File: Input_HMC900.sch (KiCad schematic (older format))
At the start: 7 parts

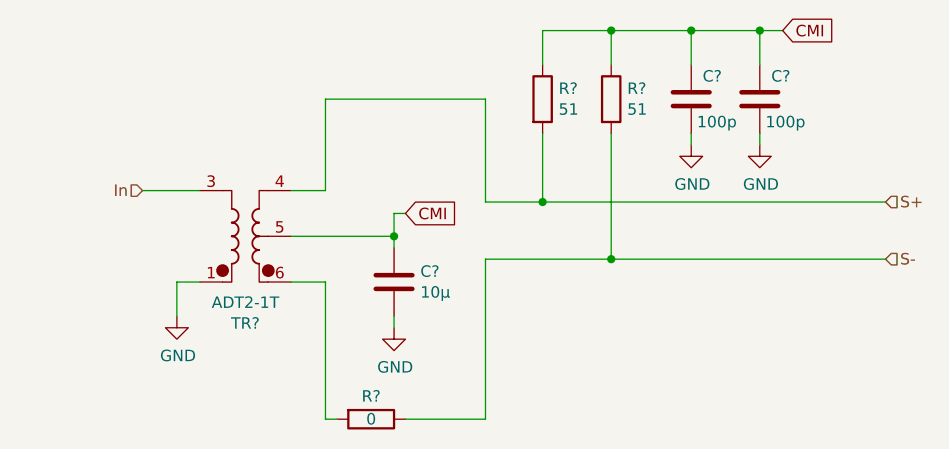
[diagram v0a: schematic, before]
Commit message: Corrected errors from single ended transition
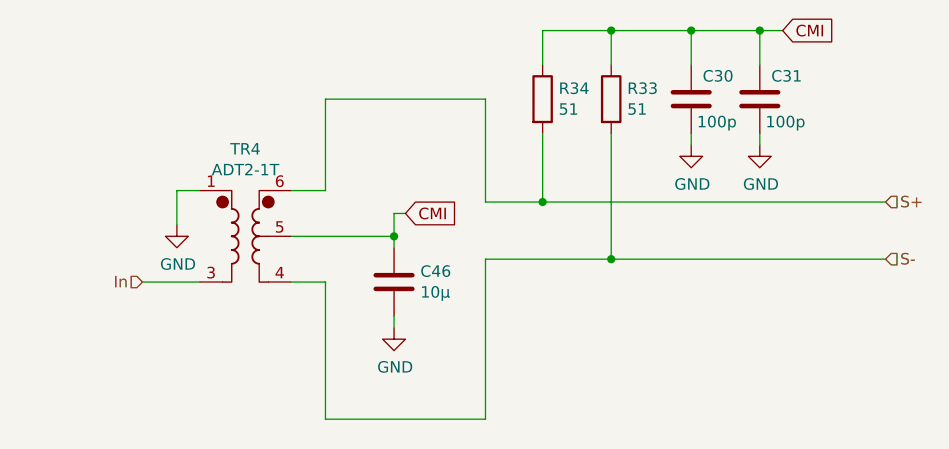
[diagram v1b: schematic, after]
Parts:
- removed R44: 0, Resistor_SMD:R_0402_1005Metric, symbol Device:R
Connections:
- net S+: now also TR4.6; no longer TR4.4
- net S-: now also TR4.4
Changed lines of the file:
@@
 $Descr A4 11693 8268
 encoding utf-8
-Sheet 4 7
+Sheet 5 7
 Title ""
 Date ""
@@
 AR Path="/60D21B6E/6110419F/60F9EBFF" Ref="C30"  Part="1"
 AR Path="/60D21B6E/61121120/60F9EBFF" Ref="C28"  Part="1"
-AR Path="/60D21B6E/60F52DEE/60F9EBFF" Ref="C?"  Part="1"
-F 0 "C?" H 6150 2800 50  0000 R CNN
+AR Path="/60D21B6E/60F52DEE/60F9EBFF" Ref="C30"  Part="1"
+F 0 "C30" H 6150 2800 50  0000 R CNN
 F 1 "100p" H 6175 3000 50  0000 R CNN
 F 2 "Capacitor_SMD:C_0402_1005Metric" H 6238 2750 50  0001 C CNN
@@
 AR Path="/60D21B6E/6110419F/60F9EC14" Ref="#PWR0135"  Part="1"
 AR Path="/60D21B6E/61121120/60F9EC14" Ref="#PWR0131"  Part="1"
-AR Path="/60D21B6E/60F52DEE/60F9EC14" Ref="#PWR?"  Part="1"
-F 0 "#PWR?" H 6200 2850 50  0001 C CNN
+AR Path="/60D21B6E/60F52DEE/60F9EC14" Ref="#PWR0135"  Part="1"
+F 0 "#PWR0135" H 6200 2850 50  0001 C CNN
 F 1 "GND" H 6205 2927 50  0000 C CNN
 F 2 "" H 6200 3100 50  0001 C CNN
@@
 	1    0    0    -1
 $EndComp
-$Comp
-L Device:R R?
-U 1 1 60F9EC7E
-P 4800 4300
-AR Path="/60D21B6E/60F9EC7E" Ref="R?"  Part="1"
-AR Path="/60D21B6E/60D894BC/60F9EC7E" Ref="R?"  Part="1"
-AR Path="/60D21B6E/6110419F/60F9EC7E" Ref="R44"  Part="1"
-AR Path="/60D21B6E/61121120/60F9EC7E" Ref="R43"  Part="1"
-AR Path="/60D21B6E/60F52DEE/60F9EC7E" Ref="R?"  Part="1"
-F 0 "R?" V 4700 4300 50  0000 C CNN
-F 1 "0" V 4800 4300 50  0000 C CNN
-F 2 "Resistor_SMD:R_0402_1005Metric" V 4730 4300 50  0001 C CNN
-F 3 "~" H 4800 4300 50  0001 C CNN
-	1    4800 4300
-	0    1    1    0
-$EndComp
 Wire Wire Line
 	5300 3600 5300 4300
-Wire Wire Line
-	4600 4300 4650 4300
-Wire Wire Line
-	4950 4300 5300 4300
 Wire Wire Line
 	5300 3600 5850 3600
@@
 AR Path="/60D21B6E/6110419F/60F9EC05" Ref="C31"  Part="1"
 AR Path="/60D21B6E/61121120/60F9EC05" Ref="C29"  Part="1"
-AR Path="/60D21B6E/60F52DEE/60F9EC05" Ref="C?"  Part="1"
-F 0 "C?" H 6450 2800 50  0000 R CNN
+AR Path="/60D21B6E/60F52DEE/60F9EC05" Ref="C31"  Part="1"
+F 0 "C31" H 6450 2800 50  0000 R CNN
 F 1 "100p" H 6475 3000 50  0000 R CNN
 F 2 "Capacitor_SMD:C_0402_1005Metric" H 6538 2750 50  0001 C CNN
@@
 AR Path="/60D21B6E/6110419F/6100BC4B" Ref="#PWR0138"  Part="1"
 AR Path="/60D21B6E/61121120/6100BC4B" Ref="#PWR0134"  Part="1"
-AR Path="/60D21B6E/60F52DEE/6100BC4B" Ref="#PWR?"  Part="1"
-F 0 "#PWR?" H 6500 2850 50  0001 C CNN
+AR Path="/60D21B6E/60F52DEE/6100BC4B" Ref="#PWR0136"  Part="1"
+F 0 "#PWR0136" H 6500 2850 50  0001 C CNN
 F 1 "GND" H 6505 2927 50  0000 C CNN
 F 2 "" H 6500 3100 50  0001 C CNN
@@
 Wire Wire Line
 	5850 3600 7050 3600
-Text HLabel 3800 3300 0    50   Input ~ 0
+Text HLabel 3800 3700 0    50   Input ~ 0
 In
 Text HLabel 7050 3350 2    50   Input ~ 0
@@
 AR Path="/60D21B6E/6110419F/60F9EBF5" Ref="R33"  Part="1"
 AR Path="/60D21B6E/61121120/60F9EBF5" Ref="R32"  Part="1"
-AR Path="/60D21B6E/60F52DEE/60F9EBF5" Ref="R?"  Part="1"
-F 0 "R?" H 5920 2946 50  0000 L CNN
+AR Path="/60D21B6E/60F52DEE/60F9EBF5" Ref="R33"  Part="1"
+F 0 "R33" H 5920 2946 50  0000 L CNN
 F 1 "51" H 5920 2855 50  0000 L CNN
 F 2 "Resistor_SMD:R_0402_1005Metric" V 5780 2900 50  0001 C CNN
@@
 AR Path="/60D21B6E/6110419F/60F9EC23" Ref="R34"  Part="1"
 AR Path="/60D21B6E/61121120/60F9EC23" Ref="R31"  Part="1"
-AR Path="/60D21B6E/60F52DEE/60F9EC23" Ref="R?"  Part="1"
-F 0 "R?" H 5620 2946 50  0000 L CNN
+AR Path="/60D21B6E/60F52DEE/60F9EC23" Ref="R34"  Part="1"
+F 0 "R34" H 5620 2946 50  0000 L CNN
 F 1 "51" H 5620 2855 50  0000 L CNN
 F 2 "Resistor_SMD:R_0402_1005Metric" V 5480 2900 50  0001 C CNN
@@
 AR Path="/60D21B6E/6110419F/60F9EC42" Ref="#PWR0137"  Part="1"
 AR Path="/60D21B6E/61121120/60F9EC42" Ref="#PWR0133"  Part="1"
-AR Path="/60D21B6E/60F52DEE/60F9EC42" Ref="#PWR?"  Part="1"
-F 0 "#PWR?" H 4900 3650 50  0001 C CNN
+AR Path="/60D21B6E/60F52DEE/60F9EC42" Ref="#PWR0137"  Part="1"
+F 0 "#PWR0137" H 4900 3650 50  0001 C CNN
 F 1 "GND" H 4905 3727 50  0000 C CNN
 F 2 "" H 4900 3900 50  0001 C CNN
@@
 	4900 3500 4900 3550
 Wire Wire Line
-	4050 3700 3950 3700
+	4050 3300 3950 3300
 $Comp
 L Device:C C?
@@
 AR Path="/60D21B6E/6110419F/60F9EC6C" Ref="C46"  Part="1"
 AR Path="/60D21B6E/61121120/60F9EC6C" Ref="C45"  Part="1"
-AR Path="/60D21B6E/60F52DEE/60F9EC6C" Ref="C?"  Part="1"
-F 0 "C?" H 4785 3654 50  0000 R CNN
+AR Path="/60D21B6E/60F52DEE/60F9EC6C" Ref="C46"  Part="1"
+F 0 "C46" H 4785 3654 50  0000 R CNN
 F 1 "10µ" H 4785 3745 50  0000 R CNN
 F 2 "Capacitor_SMD:C_0402_1005Metric" H 4938 3550 50  0001 C CNN
@@
 AR Path="/60D21B6E/6110419F/60F9EC66" Ref="TR4"  Part="1"
 AR Path="/60D21B6E/61121120/60F9EC66" Ref="TR3"  Part="1"
-AR Path="/60D21B6E/60F52DEE/60F9EC66" Ref="TR?"  Part="1"
-F 0 "TR?" H 4250 3881 50  0000 C CNN
+AR Path="/60D21B6E/60F52DEE/60F9EC66" Ref="TR4"  Part="1"
+F 0 "TR4" H 4250 3881 50  0000 C CNN
 F 1 "ADT2-1T" H 4250 3790 50  0000 C CNN
 F 2 "RF_Mini-Circuits:Mini-Circuits_CD542_H2.84mm" H 4250 3150 50  0001 C CNN
 F 3 "https://www.minicircuits.com/pdfs/ADT2-1T+.pdf" H 4250 3500 50  0001 C CNN
 	1    4250 3500
-	1    0    0    1
+	1    0    0    -1
 $EndComp
 Wire Wire Line
@@
 Connection ~ 5550 3350
 Wire Wire Line
-	3800 3300 4050 3300
+	3800 3700 4050 3700
 Wire Wire Line
 	4450 3300 4600 3300
@@
 	4450 3500 4900 3500
 Wire Wire Line
-	3950 3700 3950 3850
+	3950 3300 3950 3450
 $Comp
 L power:GND #PWR?
 U 1 1 60F9EC3C
-P 3950 3850
+P 3950 3450
 AR Path="/60D21B6E/60F9EC3C" Ref="#PWR?"  Part="1"
 AR Path="/60D21B6E/60D894BC/60F9EC3C" Ref="#PWR?"  Part="1"
 AR Path="/60D21B6E/6110419F/60F9EC3C" Ref="#PWR0136"  Part="1"
 AR Path="/60D21B6E/61121120/60F9EC3C" Ref="#PWR0132"  Part="1"
-AR Path="/60D21B6E/60F52DEE/60F9EC3C" Ref="#PWR?"  Part="1"
-F 0 "#PWR?" H 3950 3600 50  0001 C CNN
-F 1 "GND" H 3955 3677 50  0000 C CNN
-F 2 "" H 3950 3850 50  0001 C CNN
-F 3 "" H 3950 3850 50  0001 C CNN
-	1    3950 3850
-	1    0    0    -1
-$EndComp
+AR Path="/60D21B6E/60F52DEE/60F9EC3C" Ref="#PWR0138"  Part="1"
+F 0 "#PWR0138" H 3950 3200 50  0001 C CNN
+F 1 "GND" H 3955 3277 50  0000 C CNN
+F 2 "" H 3950 3450 50  0001 C CNN
+F 3 "" H 3950 3450 50  0001 C CNN
+	1    3950 3450
+	1    0    0    -1
+$EndComp
+Wire Wire Line
+	4600 4300 5300 4300
 $EndSCHEMATC

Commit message: passage 0402 => 0603
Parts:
- C30, C31, C46: footprint Capacitor_SMD:C_0402_1005Metric -> Capacitor_SMD:C_0603_1608Metric_Pad1.08x0.95mm_HandSolder
- R33, R34: footprint Resistor_SMD:R_0402_1005Metric -> Resistor_SMD:R_0603_1608Metric_Pad0.98x0.95mm_HandSolder
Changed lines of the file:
@@
 $Descr A4 11693 8268
 encoding utf-8
-Sheet 5 7
+Sheet 4 7
 Title ""
 Date ""
@@
 AR Path="/60D21B6E/61121120/60F9EBFF" Ref="C28"  Part="1"
 AR Path="/60D21B6E/60F52DEE/60F9EBFF" Ref="C30"  Part="1"
-F 0 "C30" H 6150 2800 50  0000 R CNN
+F 0 "C28" H 6150 2800 50  0000 R CNN
 F 1 "100p" H 6175 3000 50  0000 R CNN
-F 2 "Capacitor_SMD:C_0402_1005Metric" H 6238 2750 50  0001 C CNN
+F 2 "Capacitor_SMD:C_0603_1608Metric_Pad1.08x0.95mm_HandSolder" H 6238 2750 50  0001 C CNN
 F 3 "~" H 6200 2900 50  0001 C CNN
 	1    6200 2900
@@
 AR Path="/60D21B6E/61121120/60F9EC05" Ref="C29"  Part="1"
 AR Path="/60D21B6E/60F52DEE/60F9EC05" Ref="C31"  Part="1"
-F 0 "C31" H 6450 2800 50  0000 R CNN
+F 0 "C29" H 6450 2800 50  0000 R CNN
 F 1 "100p" H 6475 3000 50  0000 R CNN
-F 2 "Capacitor_SMD:C_0402_1005Metric" H 6538 2750 50  0001 C CNN
+F 2 "Capacitor_SMD:C_0603_1608Metric_Pad1.08x0.95mm_HandSolder" H 6538 2750 50  0001 C CNN
 F 3 "~" H 6500 2900 50  0001 C CNN
 	1    6500 2900
@@
 AR Path="/60D21B6E/61121120/60F9EBF5" Ref="R32"  Part="1"
 AR Path="/60D21B6E/60F52DEE/60F9EBF5" Ref="R33"  Part="1"
-F 0 "R33" H 5920 2946 50  0000 L CNN
+F 0 "R32" H 5920 2946 50  0000 L CNN
 F 1 "51" H 5920 2855 50  0000 L CNN
-F 2 "Resistor_SMD:R_0402_1005Metric" V 5780 2900 50  0001 C CNN
+F 2 "Resistor_SMD:R_0603_1608Metric_Pad0.98x0.95mm_HandSolder" V 5780 2900 50  0001 C CNN
 F 3 "~" H 5850 2900 50  0001 C CNN
 	1    5850 2900
@@
 AR Path="/60D21B6E/61121120/60F9EC23" Ref="R31"  Part="1"
 AR Path="/60D21B6E/60F52DEE/60F9EC23" Ref="R34"  Part="1"
-F 0 "R34" H 5620 2946 50  0000 L CNN
+F 0 "R31" H 5620 2946 50  0000 L CNN
 F 1 "51" H 5620 2855 50  0000 L CNN
-F 2 "Resistor_SMD:R_0402_1005Metric" V 5480 2900 50  0001 C CNN
+F 2 "Resistor_SMD:R_0603_1608Metric_Pad0.98x0.95mm_HandSolder" V 5480 2900 50  0001 C CNN
 F 3 "~" H 5550 2900 50  0001 C CNN
 	1    5550 2900
@@
 AR Path="/60D21B6E/61121120/60F9EC6C" Ref="C45"  Part="1"
 AR Path="/60D21B6E/60F52DEE/60F9EC6C" Ref="C46"  Part="1"
-F 0 "C46" H 4785 3654 50  0000 R CNN
+F 0 "C45" H 4785 3654 50  0000 R CNN
 F 1 "10µ" H 4785 3745 50  0000 R CNN
-F 2 "Capacitor_SMD:C_0402_1005Metric" H 4938 3550 50  0001 C CNN
+F 2 "Capacitor_SMD:C_0603_1608Metric_Pad1.08x0.95mm_HandSolder" H 4938 3550 50  0001 C CNN
 F 3 "~" H 4900 3700 50  0001 C CNN
 	1    4900 3700
@@
 AR Path="/60D21B6E/61121120/60F9EC66" Ref="TR3"  Part="1"
 AR Path="/60D21B6E/60F52DEE/60F9EC66" Ref="TR4"  Part="1"
-F 0 "TR4" H 4250 3881 50  0000 C CNN
+F 0 "TR3" H 4250 3881 50  0000 C CNN
 F 1 "ADT2-1T" H 4250 3790 50  0000 C CNN
 F 2 "RF_Mini-Circuits:Mini-Circuits_CD542_H2.84mm" H 4250 3150 50  0001 C CNN

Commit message: Changed transfo reference from gnd to 2.5v because ds1085 goes from 0 to 5v
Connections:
- net CMI: now also TR4.1
- net GND: no longer TR4.1
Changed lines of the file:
@@
 AR Path="/60D21B6E/61121120/60F9EC14" Ref="#PWR0131"  Part="1"
 AR Path="/60D21B6E/60F52DEE/60F9EC14" Ref="#PWR0135"  Part="1"
-F 0 "#PWR0135" H 6200 2850 50  0001 C CNN
+F 0 "#PWR0131" H 6200 2850 50  0001 C CNN
 F 1 "GND" H 6205 2927 50  0000 C CNN
 F 2 "" H 6200 3100 50  0001 C CNN
@@
 AR Path="/60D21B6E/61121120/6100BC4B" Ref="#PWR0134"  Part="1"
 AR Path="/60D21B6E/60F52DEE/6100BC4B" Ref="#PWR0136"  Part="1"
-F 0 "#PWR0136" H 6500 2850 50  0001 C CNN
+F 0 "#PWR0134" H 6500 2850 50  0001 C CNN
 F 1 "GND" H 6505 2927 50  0000 C CNN
 F 2 "" H 6500 3100 50  0001 C CNN
@@
 AR Path="/60D21B6E/61121120/60F9EC42" Ref="#PWR0133"  Part="1"
 AR Path="/60D21B6E/60F52DEE/60F9EC42" Ref="#PWR0137"  Part="1"
-F 0 "#PWR0137" H 4900 3650 50  0001 C CNN
+F 0 "#PWR0133" H 4900 3650 50  0001 C CNN
 F 1 "GND" H 4905 3727 50  0000 C CNN
 F 2 "" H 4900 3900 50  0001 C CNN
@@
 	4450 3500 4900 3500
 Wire Wire Line
-	3950 3300 3950 3450
-$Comp
-L power:GND #PWR?
-U 1 1 60F9EC3C
-P 3950 3450
-AR Path="/60D21B6E/60F9EC3C" Ref="#PWR?"  Part="1"
-AR Path="/60D21B6E/60D894BC/60F9EC3C" Ref="#PWR?"  Part="1"
-AR Path="/60D21B6E/6110419F/60F9EC3C" Ref="#PWR0136"  Part="1"
-AR Path="/60D21B6E/61121120/60F9EC3C" Ref="#PWR0132"  Part="1"
-AR Path="/60D21B6E/60F52DEE/60F9EC3C" Ref="#PWR0138"  Part="1"
-F 0 "#PWR0138" H 3950 3200 50  0001 C CNN
-F 1 "GND" H 3955 3277 50  0000 C CNN
-F 2 "" H 3950 3450 50  0001 C CNN
-F 3 "" H 3950 3450 50  0001 C CNN
-	1    3950 3450
-	1    0    0    -1
-$EndComp
-Wire Wire Line
 	4600 4300 5300 4300
+Text GLabel 3950 3300 0    50   Input ~ 0
+CMI
 $EndSCHEMATC

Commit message: Made it so there was only one output and change the SMA (to a sourceable one)
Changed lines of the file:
@@
 AR Path="/60D21B6E/61121120/60F9EBFF" Ref="C28"  Part="1"
 AR Path="/60D21B6E/60F52DEE/60F9EBFF" Ref="C30"  Part="1"
-F 0 "C28" H 6150 2800 50  0000 R CNN
+F 0 "C30" H 6150 2800 50  0000 R CNN
 F 1 "100p" H 6175 3000 50  0000 R CNN
 F 2 "Capacitor_SMD:C_0603_1608Metric_Pad1.08x0.95mm_HandSolder" H 6238 2750 50  0001 C CNN
@@
 AR Path="/60D21B6E/61121120/60F9EC14" Ref="#PWR0131"  Part="1"
 AR Path="/60D21B6E/60F52DEE/60F9EC14" Ref="#PWR0135"  Part="1"
-F 0 "#PWR0131" H 6200 2850 50  0001 C CNN
+F 0 "#PWR0135" H 6200 2850 50  0001 C CNN
 F 1 "GND" H 6205 2927 50  0000 C CNN
 F 2 "" H 6200 3100 50  0001 C CNN
@@
 AR Path="/60D21B6E/61121120/60F9EC05" Ref="C29"  Part="1"
 AR Path="/60D21B6E/60F52DEE/60F9EC05" Ref="C31"  Part="1"
-F 0 "C29" H 6450 2800 50  0000 R CNN
+F 0 "C31" H 6450 2800 50  0000 R CNN
 F 1 "100p" H 6475 3000 50  0000 R CNN
 F 2 "Capacitor_SMD:C_0603_1608Metric_Pad1.08x0.95mm_HandSolder" H 6538 2750 50  0001 C CNN
@@
 AR Path="/60D21B6E/61121120/6100BC4B" Ref="#PWR0134"  Part="1"
 AR Path="/60D21B6E/60F52DEE/6100BC4B" Ref="#PWR0136"  Part="1"
-F 0 "#PWR0134" H 6500 2850 50  0001 C CNN
+F 0 "#PWR0136" H 6500 2850 50  0001 C CNN
 F 1 "GND" H 6505 2927 50  0000 C CNN
 F 2 "" H 6500 3100 50  0001 C CNN
@@
 AR Path="/60D21B6E/61121120/60F9EBF5" Ref="R32"  Part="1"
 AR Path="/60D21B6E/60F52DEE/60F9EBF5" Ref="R33"  Part="1"
-F 0 "R32" H 5920 2946 50  0000 L CNN
+F 0 "R33" H 5920 2946 50  0000 L CNN
 F 1 "51" H 5920 2855 50  0000 L CNN
 F 2 "Resistor_SMD:R_0603_1608Metric_Pad0.98x0.95mm_HandSolder" V 5780 2900 50  0001 C CNN
@@
 AR Path="/60D21B6E/61121120/60F9EC23" Ref="R31"  Part="1"
 AR Path="/60D21B6E/60F52DEE/60F9EC23" Ref="R34"  Part="1"
-F 0 "R31" H 5620 2946 50  0000 L CNN
+F 0 "R34" H 5620 2946 50  0000 L CNN
 F 1 "51" H 5620 2855 50  0000 L CNN
 F 2 "Resistor_SMD:R_0603_1608Metric_Pad0.98x0.95mm_HandSolder" V 5480 2900 50  0001 C CNN
@@
 AR Path="/60D21B6E/61121120/60F9EC42" Ref="#PWR0133"  Part="1"
 AR Path="/60D21B6E/60F52DEE/60F9EC42" Ref="#PWR0137"  Part="1"
-F 0 "#PWR0133" H 4900 3650 50  0001 C CNN
+F 0 "#PWR0137" H 4900 3650 50  0001 C CNN
 F 1 "GND" H 4905 3727 50  0000 C CNN
 F 2 "" H 4900 3900 50  0001 C CNN
@@
 AR Path="/60D21B6E/61121120/60F9EC6C" Ref="C45"  Part="1"
 AR Path="/60D21B6E/60F52DEE/60F9EC6C" Ref="C46"  Part="1"
-F 0 "C45" H 4785 3654 50  0000 R CNN
+F 0 "C46" H 4785 3654 50  0000 R CNN
 F 1 "10µ" H 4785 3745 50  0000 R CNN
 F 2 "Capacitor_SMD:C_0603_1608Metric_Pad1.08x0.95mm_HandSolder" H 4938 3550 50  0001 C CNN
@@
 AR Path="/60D21B6E/61121120/60F9EC66" Ref="TR3"  Part="1"
 AR Path="/60D21B6E/60F52DEE/60F9EC66" Ref="TR4"  Part="1"
-F 0 "TR3" H 4250 3881 50  0000 C CNN
+F 0 "TR4" H 4250 3881 50  0000 C CNN
 F 1 "ADT2-1T" H 4250 3790 50  0000 C CNN
 F 2 "RF_Mini-Circuits:Mini-Circuits_CD542_H2.84mm" H 4250 3150 50  0001 C CNN

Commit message: Changed input transformer reference to 2.5v
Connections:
- net CMI: now also TR4.3; no longer TR4.1
- net In: now also TR4.1; no longer TR4.3
- net S+: now also TR4.4; no longer TR4.6
- net S-: now also TR4.6; no longer TR4.4
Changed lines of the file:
@@
 $Descr A4 11693 8268
 encoding utf-8
-Sheet 4 7
+Sheet 5 7
 Title ""
 Date ""
@@
 F 3 "https://www.minicircuits.com/pdfs/ADT2-1T+.pdf" H 4250 3500 50  0001 C CNN
 	1    4250 3500
-	1    0    0    -1
-$EndComp
-Wire Wire Line
+	1    0    0    1
+$EndComp
+Wire Wire Line

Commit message: Straitened things before restarting routing
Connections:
- net CMI: now also TR4.1; no longer TR4.3
- net In: now also TR4.3; no longer TR4.1
- net S+: now also TR4.6; no longer TR4.4
- net S-: now also TR4.4; no longer TR4.6
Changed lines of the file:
@@
 $Descr A4 11693 8268
 encoding utf-8
-Sheet 5 7
+Sheet 4 7
 Title ""
 Date ""
@@
 AR Path="/60D21B6E/61121120/60F9EBFF" Ref="C28"  Part="1"
 AR Path="/60D21B6E/60F52DEE/60F9EBFF" Ref="C30"  Part="1"
-F 0 "C30" H 6150 2800 50  0000 R CNN
+F 0 "C28" H 6150 2800 50  0000 R CNN
 F 1 "100p" H 6175 3000 50  0000 R CNN
 F 2 "Capacitor_SMD:C_0603_1608Metric_Pad1.08x0.95mm_HandSolder" H 6238 2750 50  0001 C CNN
@@
 AR Path="/60D21B6E/61121120/60F9EC05" Ref="C29"  Part="1"
 AR Path="/60D21B6E/60F52DEE/60F9EC05" Ref="C31"  Part="1"
-F 0 "C31" H 6450 2800 50  0000 R CNN
+F 0 "C29" H 6450 2800 50  0000 R CNN
 F 1 "100p" H 6475 3000 50  0000 R CNN
 F 2 "Capacitor_SMD:C_0603_1608Metric_Pad1.08x0.95mm_HandSolder" H 6538 2750 50  0001 C CNN
@@
 AR Path="/60D21B6E/61121120/60F9EBF5" Ref="R32"  Part="1"
 AR Path="/60D21B6E/60F52DEE/60F9EBF5" Ref="R33"  Part="1"
-F 0 "R33" H 5920 2946 50  0000 L CNN
+F 0 "R32" H 5920 2946 50  0000 L CNN
 F 1 "51" H 5920 2855 50  0000 L CNN
 F 2 "Resistor_SMD:R_0603_1608Metric_Pad0.98x0.95mm_HandSolder" V 5780 2900 50  0001 C CNN
@@
 AR Path="/60D21B6E/61121120/60F9EC23" Ref="R31"  Part="1"
 AR Path="/60D21B6E/60F52DEE/60F9EC23" Ref="R34"  Part="1"
-F 0 "R34" H 5620 2946 50  0000 L CNN
+F 0 "R31" H 5620 2946 50  0000 L CNN
 F 1 "51" H 5620 2855 50  0000 L CNN
 F 2 "Resistor_SMD:R_0603_1608Metric_Pad0.98x0.95mm_HandSolder" V 5480 2900 50  0001 C CNN
@@
 AR Path="/60D21B6E/61121120/60F9EC6C" Ref="C45"  Part="1"
 AR Path="/60D21B6E/60F52DEE/60F9EC6C" Ref="C46"  Part="1"
-F 0 "C46" H 4785 3654 50  0000 R CNN
+F 0 "C45" H 4785 3654 50  0000 R CNN
 F 1 "10µ" H 4785 3745 50  0000 R CNN
 F 2 "Capacitor_SMD:C_0603_1608Metric_Pad1.08x0.95mm_HandSolder" H 4938 3550 50  0001 C CNN
@@
 AR Path="/60D21B6E/61121120/60F9EC66" Ref="TR3"  Part="1"
 AR Path="/60D21B6E/60F52DEE/60F9EC66" Ref="TR4"  Part="1"
-F 0 "TR4" H 4250 3881 50  0000 C CNN
+F 0 "TR3" H 4250 3881 50  0000 C CNN
 F 1 "ADT2-1T" H 4250 3790 50  0000 C CNN
 F 2 "RF_Mini-Circuits:Mini-Circuits_CD542_H2.84mm" H 4250 3150 50  0001 C CNN
 F 3 "https://www.minicircuits.com/pdfs/ADT2-1T+.pdf" H 4250 3500 50  0001 C CNN
 	1    4250 3500
-	1    0    0    1
-$EndComp
-Wire Wire Line
+	1    0    0    -1
+$EndComp
+Wire Wire Line

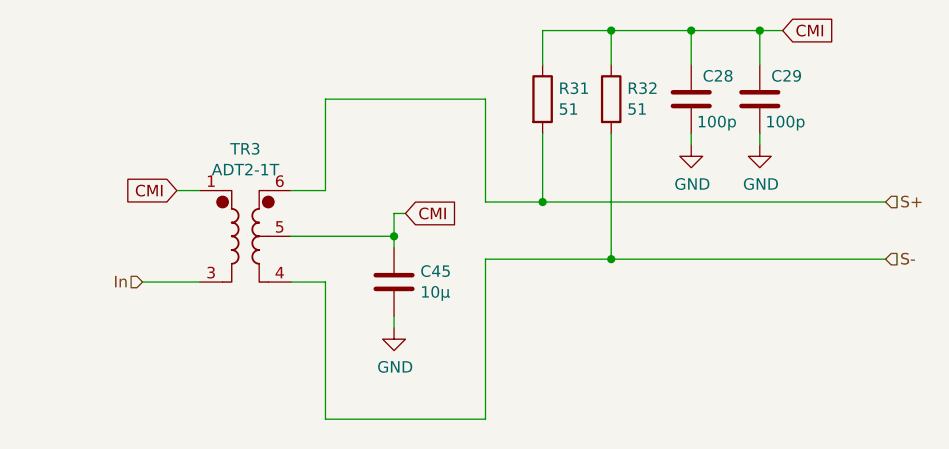
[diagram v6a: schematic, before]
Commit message: Added Logic gate buffer for the oscillator
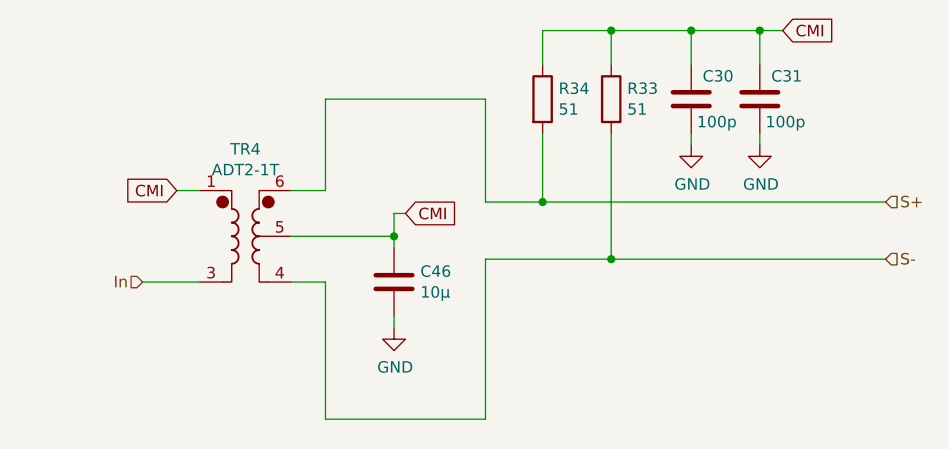
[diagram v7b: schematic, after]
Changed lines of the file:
@@
 $Descr A4 11693 8268
 encoding utf-8
-Sheet 4 7
+Sheet 5 7
 Title ""
 Date ""
@@
 AR Path="/60D21B6E/61121120/60F9EBFF" Ref="C28"  Part="1"
 AR Path="/60D21B6E/60F52DEE/60F9EBFF" Ref="C30"  Part="1"
-F 0 "C28" H 6150 2800 50  0000 R CNN
+F 0 "C30" H 6150 2800 50  0000 R CNN
 F 1 "100p" H 6175 3000 50  0000 R CNN
 F 2 "Capacitor_SMD:C_0603_1608Metric_Pad1.08x0.95mm_HandSolder" H 6238 2750 50  0001 C CNN
@@
 AR Path="/60D21B6E/61121120/60F9EC05" Ref="C29"  Part="1"
 AR Path="/60D21B6E/60F52DEE/60F9EC05" Ref="C31"  Part="1"
-F 0 "C29" H 6450 2800 50  0000 R CNN
+F 0 "C31" H 6450 2800 50  0000 R CNN
 F 1 "100p" H 6475 3000 50  0000 R CNN
 F 2 "Capacitor_SMD:C_0603_1608Metric_Pad1.08x0.95mm_HandSolder" H 6538 2750 50  0001 C CNN
@@
 AR Path="/60D21B6E/61121120/60F9EBF5" Ref="R32"  Part="1"
 AR Path="/60D21B6E/60F52DEE/60F9EBF5" Ref="R33"  Part="1"
-F 0 "R32" H 5920 2946 50  0000 L CNN
+F 0 "R33" H 5920 2946 50  0000 L CNN
 F 1 "51" H 5920 2855 50  0000 L CNN
 F 2 "Resistor_SMD:R_0603_1608Metric_Pad0.98x0.95mm_HandSolder" V 5780 2900 50  0001 C CNN
@@
 AR Path="/60D21B6E/61121120/60F9EC23" Ref="R31"  Part="1"
 AR Path="/60D21B6E/60F52DEE/60F9EC23" Ref="R34"  Part="1"
-F 0 "R31" H 5620 2946 50  0000 L CNN
+F 0 "R34" H 5620 2946 50  0000 L CNN
 F 1 "51" H 5620 2855 50  0000 L CNN
 F 2 "Resistor_SMD:R_0603_1608Metric_Pad0.98x0.95mm_HandSolder" V 5480 2900 50  0001 C CNN
@@
 AR Path="/60D21B6E/61121120/60F9EC6C" Ref="C45"  Part="1"
 AR Path="/60D21B6E/60F52DEE/60F9EC6C" Ref="C46"  Part="1"
-F 0 "C45" H 4785 3654 50  0000 R CNN
+F 0 "C46" H 4785 3654 50  0000 R CNN
 F 1 "10µ" H 4785 3745 50  0000 R CNN
 F 2 "Capacitor_SMD:C_0603_1608Metric_Pad1.08x0.95mm_HandSolder" H 4938 3550 50  0001 C CNN
@@
 AR Path="/60D21B6E/61121120/60F9EC66" Ref="TR3"  Part="1"
 AR Path="/60D21B6E/60F52DEE/60F9EC66" Ref="TR4"  Part="1"
-F 0 "TR3" H 4250 3881 50  0000 C CNN
+F 0 "TR4" H 4250 3881 50  0000 C CNN
 F 1 "ADT2-1T" H 4250 3790 50  0000 C CNN
 F 2 "RF_Mini-Circuits:Mini-Circuits_CD542_H2.84mm" H 4250 3150 50  0001 C CNN
